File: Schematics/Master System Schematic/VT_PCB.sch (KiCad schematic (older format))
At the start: 34 parts, among them K18 Voltage Tap Relay, K19 Voltage Tap Relay, K20 Voltage Tap Relay, K21 Voltage Tap Relay, K22 Voltage Tap Relay, K28 Voltage Tap Relay, K29 Voltage Tap Relay, K30 Voltage Tap Relay, K31 Voltage Tap Relay, K32 Voltage Tap Relay

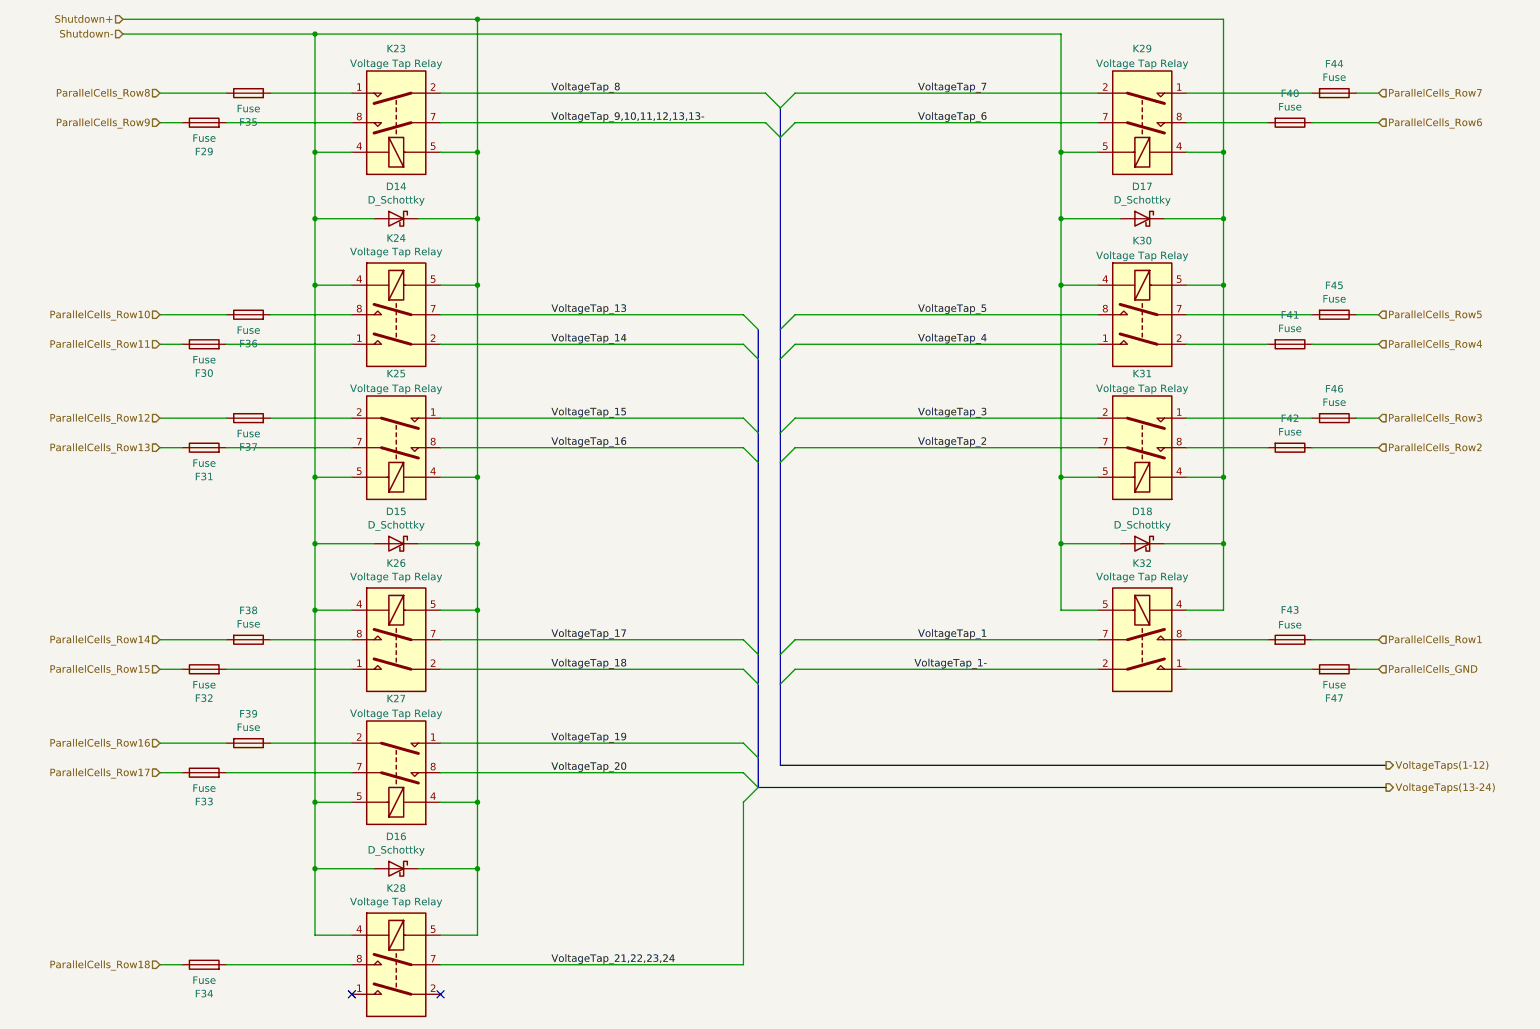
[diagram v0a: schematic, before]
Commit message: Had to refactor all IDs
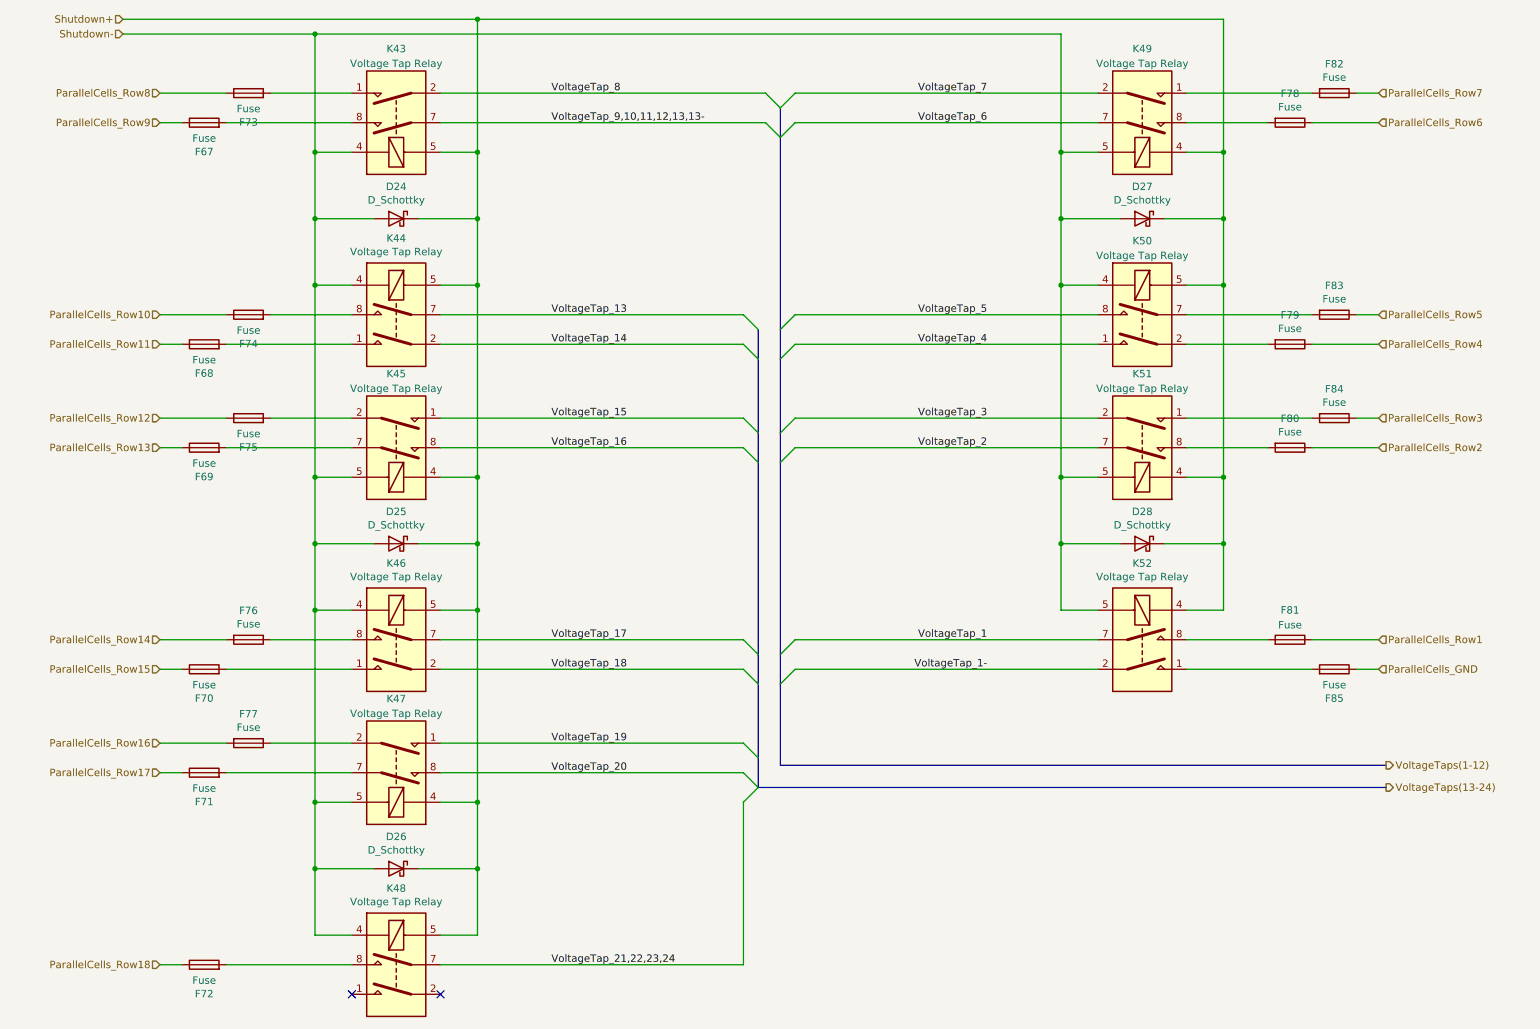
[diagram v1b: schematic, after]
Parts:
- renumbered D15 to D10, D16 to D11, D17 to D12, D18 to D13, D14 to D9, F21 to F10, F20 to F11, F19 to F12, F18 to F13, F36 to F14, F45 to F15, F12 to F16, F11 to F17, F10 to F18, F50 to F19, F55 to F20, F13 to F21, F14 to F22, F15 to F23, F16 to F24, F22 to F25, F23 to F26, F24 to F27, F25 to F28, K28 to K13, K18 to K14, K19 to K15, K20 to K16, K21 to K17, K22 to K18, K29 to K19, K30 to K20, K31 to K21, K32 to K22
